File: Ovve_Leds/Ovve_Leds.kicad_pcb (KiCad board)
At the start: 2 copper layers, 205.5 x 150 mm, 57 parts, among them J2 Conn_01x04, J3 Conn_01x04, J4 Conn_01x04, J8 Conn_01x02, U1 74LS174

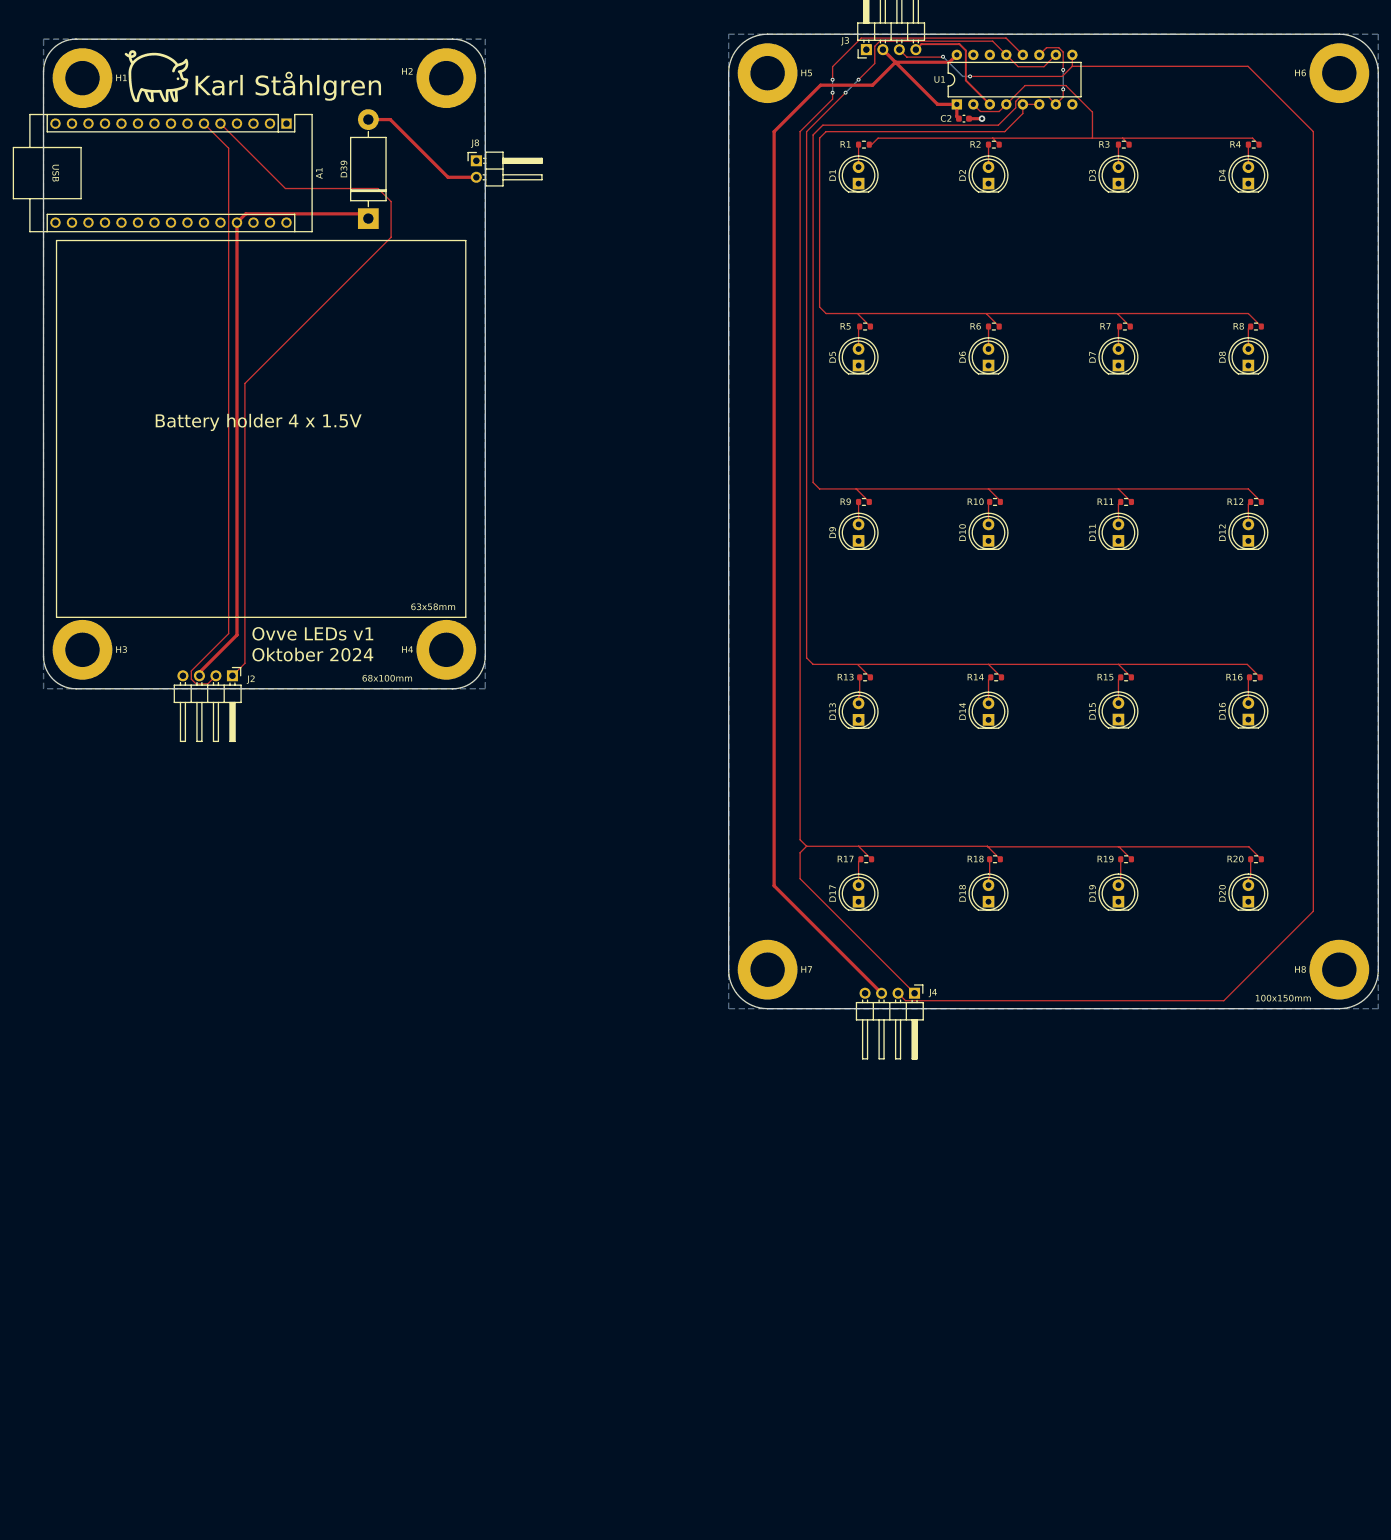
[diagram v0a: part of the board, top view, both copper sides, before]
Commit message: added mouse bites
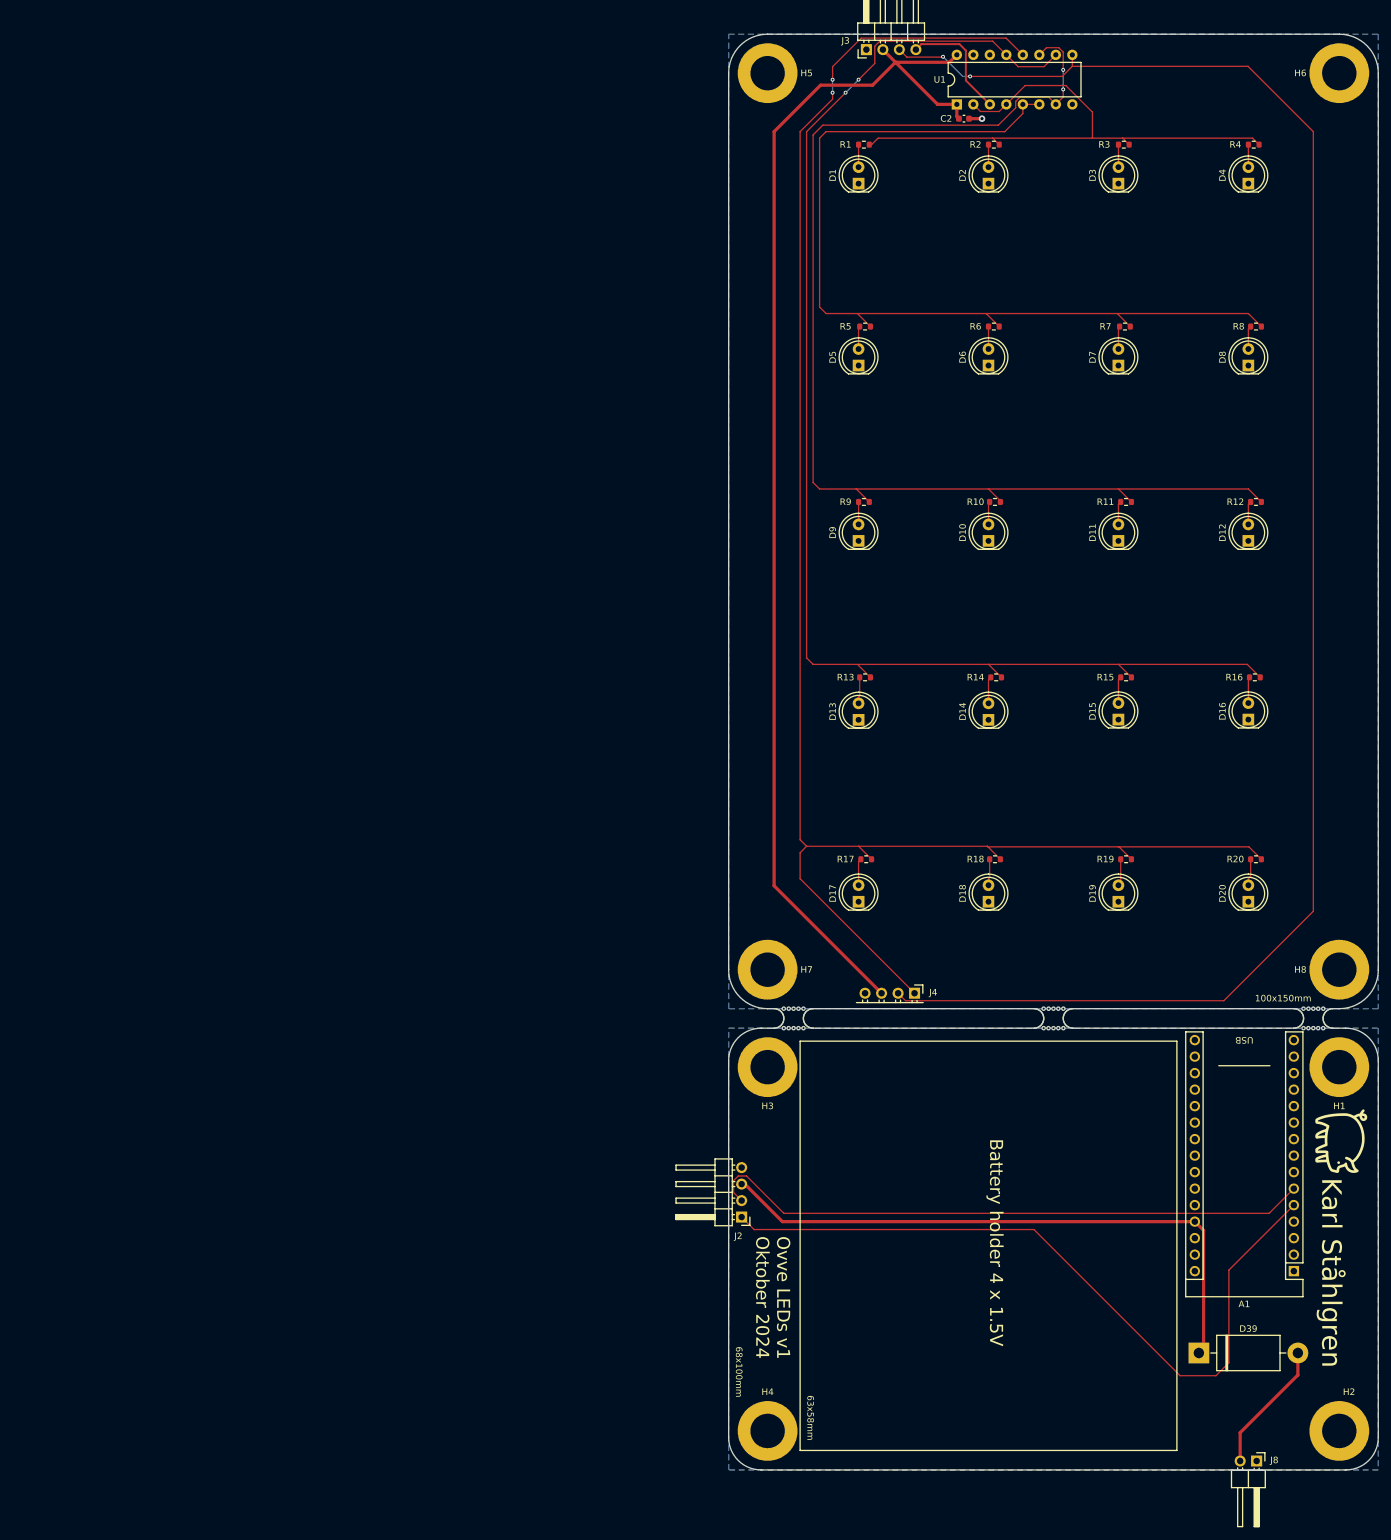
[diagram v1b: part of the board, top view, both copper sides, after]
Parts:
- added mouse-bite-3mm-slot: VAL**, Panelization:mouse-bite-3mm-slot, F.Cu at (255.0, 306.5)
- added mouse-bite-3mm-slot: VAL**, Panelization:mouse-bite-3mm-slot, F.Cu at (295.0, 306.5)
- added mouse-bite-3mm-slot: VAL**, Panelization:mouse-bite-3mm-slot, F.Cu at (215.0, 306.5)
- moved H2 249.5 mm to (299.0, 370.0), turned to -90 degrees
- moved H1 246.2 mm to (299.0, 314.0), turned to -90 degrees
- moved G*** 245.5 mm to (299.5, 325.5), turned to -90 degrees
- moved A1 235.0 mm to (292.0, 345.4), turned to 180 degrees
- moved J8 233.4 mm to (286.3, 374.6), turned to -90 degrees
- moved D39 216.4 mm to (277.4, 358.0), turned to 0 degrees
- moved H4 130.0 mm to (211.0, 370.0), turned to -90 degrees
- moved H3 123.5 mm to (211.0, 314.0), turned to -90 degrees
- moved J2 114.4 mm to (207.0, 337.1), turned to 180 degrees
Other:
- board size 205.5 x 150 mm -> 100 x 221 mm
